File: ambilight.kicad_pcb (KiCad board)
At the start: 2 copper layers, 12 parts, among them J1 RGB Connector, J2 USB_C, J3 USB4085-GF-A, U1 ESP-01v090, U2 AZ1117CR-3.3TRG1, U2 LD1117V33, U3 FT230XS, U4 AZ1117CR-3.3TRG1

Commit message: Bunch of updates and beginning of PCB layout
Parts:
- removed the U2 at (94.0, 45.0)
- removed the U2 at (116.5, 45.1)
- removed U4: AZ1117CR-3.3TRG1, Package_TO_SOT_SMD:SOT-89-3_Handsoldering
- added C3: 0.1uF, Capacitor_SMD:C_0805_2012Metric, F.Cu at (62.5, 38.5)
- added C4: 0.1uF, Capacitor_SMD:C_0805_2012Metric, F.Cu at (62.5, 30.5)
- added C5: 10uF, Capacitor_SMD:C_0805_2012Metric, F.Cu at (62.5, 32.5)
- added C6: TBD, Capacitor_SMD:C_0805_2012Metric, F.Cu at (82.0, 34.7)
- added C7: TBD, Capacitor_SMD:C_0805_2012Metric, F.Cu at (82.0, 40.7)
- added C8: 0.1uF, Capacitor_SMD:C_0805_2012Metric, F.Cu at (108.0, 77.5)
- added C9: 1uF, Capacitor_SMD:C_0805_2012Metric, F.Cu at (108.5, 72.0)
- added D1: LED, LED_SMD:LED_0805_2012Metric, F.Cu at (86.0, 49.4)
- added R3: 120R, Resistor_SMD:R_0805_2012Metric, F.Cu at (84.0, 49.4)
- added R4: 10kR, Resistor_SMD:R_0805_2012Metric, F.Cu at (62.5, 36.5)
- added R5: 10kR, Resistor_SMD:R_0805_2012Metric, F.Cu at (62.5, 34.5)
- added R6: 10kR, Resistor_SMD:R_0805_2012Metric, F.Cu at (68.6, 42.0)
- added R7: 0R, Resistor_SMD:R_0805_2012Metric, F.Cu at (80.0, 36.7)
- added R8: 0R, Resistor_SMD:R_0805_2012Metric, F.Cu at (80.0, 38.7)
- added SW1: RESET, Button_Switch_SMD:SW_Push_1P1T_NO_CK_KMR2, F.Cu at (62.5, 44.8)
- added SW2: BOOT, Button_Switch_SMD:SW_Push_1P1T_NO_CK_KMR2, F.Cu at (68.5, 44.8)
- added TP1: ~, Custom_PCBWay:TestPoint_Pad_D2.5mm_SilkscreenFix, F.Cu at (89.0, 45.5)
- added TP2: ~, Custom_PCBWay:TestPoint_Pad_D2.5mm_SilkscreenFix, F.Cu at (80.0, 31.5)
- added TP3: ~, Custom_PCBWay:TestPoint_Pad_D2.5mm_SilkscreenFix, F.Cu at (86.0, 31.5)
- added TP4: ~, Custom_PCBWay:TestPoint_Pad_D2.5mm_SilkscreenFix, F.Cu at (107.0, 57.5)
- added TP5: ~, Custom_PCBWay:TestPoint_Pad_D2.5mm_SilkscreenFix, F.Cu at (119.0, 60.5)
- added U2: ESP32-C3-MINI-1-H4, PCM_Espressif:ESP32-C3-MINI-1, F.Cu at (71.2, 32.2)
- C1: value 100u -> 10uF; footprint Capacitor_THT:C_Rect_L9.0mm_W2.7mm_P7.50mm_MKT -> Capacitor_SMD:C_0805_2012Metric
- C2: value 47u -> 22uF; footprint Capacitor_THT:CP_Radial_D12.5mm_P5.00mm -> Capacitor_SMD:C_0805_2012Metric
- J1: value RGB Connector -> TYPE-C-31-M-12; footprint Connector_PinHeader_2.54mm:PinHeader_1x03_P2.54mm_Vertical -> Connector_USB:USB_C_Receptacle_HRO_TYPE-C-31-M-12
- J2: value USB_C -> RGB Connector; footprint Connector_USB:USB_C_Receptacle_GCT_USB4085 -> Connector_PinHeader_2.54mm:PinHeader_1x03_P2.54mm_Vertical
- J3: value USB4085-GF-A -> Power Connector; footprint Connector_USB:USB_C_Receptacle_GCT_USB4085 -> Connector_PinHeader_2.54mm:PinHeader_1x03_P2.54mm_Vertical
- R1: value 3.8R ? -> 5.1kR; footprint Resistor_THT:R_Axial_DIN0309_L9.0mm_D3.2mm_P2.54mm_Vertical -> Resistor_SMD:R_0805_2012Metric
- R2: value 5R ? -> 5.1kR; footprint Resistor_THT:R_Axial_DIN0309_L9.0mm_D3.2mm_P2.54mm_Vertical -> Resistor_SMD:R_0805_2012Metric
- U1: value ESP-01v090 -> AZ1117CR-3.3TRG1; footprint ESP8266:ESP-01 -> Package_TO_SOT_SMD:SOT-89-3_Handsoldering
- U3: value FT230XS -> MCP1416; footprint Package_SO:SSOP-16_3.9x4.9mm_P0.635mm -> Package_TO_SOT_SMD:SOT-23-5
- moved R2 100.6 mm to (85.4, 36.4), turned to 180 degrees
- moved R1 98.8 mm to (85.4, 39.0), turned to 180 degrees
- moved J1 71.7 mm to (92.5, 38.2), turned to 90 degrees
- moved C1 63.1 mm to (82.0, 49.5)
- moved U1 57.3 mm to (77.0, 49.0), turned to 180 degrees
- moved C2 56.5 mm to (72.5, 50.0), turned to -90 degrees
- moved J3 43.7 mm to (85.5, 58.0), turned to 90 degrees
- moved J2 31.6 mm to (95.0, 52.5), turned to 0 degrees
- moved U3 10.8 mm to (76.9, 42.5), turned to 180 degrees
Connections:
- C1 pad 1: Net-(J1-Pin_3) -> VCC
- C1 pad 2: Net-(J1-Pin_1) -> GND
- C2 pad 1: Net-(U1-VCC) -> +3V3
- C2 pad 2: Net-(J1-Pin_3) -> GND
- R1 pad 1: Net-(U1-VCC) -> Net-(J1-CC1)
- R1 pad 2: Net-(J1-Pin_2) -> GND
- R2 pad 1: Net-(U1-CH_PD) -> Net-(J1-CC2)
- R2 pad 2: Net-(U1-VCC) -> GND
- U1 pad 1: unconnected-(U1-UTXD-Pad1) -> GND
- U1 pad 2: Net-(J1-Pin_3) -> +3V3
- U1 pad 3: Net-(U1-CH_PD) -> VCC
- U3 pad 2: unconnected-(U3-~{RTS}-Pad2) -> VCC
- U3 pad 3: Net-(U3-3V3OUT) -> Net-(U2-GPIO4/ADC1_CH4)
- U3 pad 4: unconnected-(U3-RXD-Pad4) -> GND
- U3 pad 5: GND -> Net-(J2-Pin_2)
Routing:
- net +3V3: track 0.00 -> 55.6 mm
- net VCC: track 0.00 -> 29.1 mm
- net GND: track 0.00 -> 22.2 mm, vias 0 -> 9
- net Net-(U2-EN/CHIP_PU): track 0.00 -> 14.3 mm
- net /USBD+: track 0.00 -> 13.3 mm
- net /USBD-: track 0.00 -> 13.1 mm
- net Net-(U2-GPIO9): track 0.00 -> 10.6 mm
- net Net-(U2-GPIO20/U0RXD): track 0.00 -> 10.3 mm
- net Net-(U2-GPIO4/ADC1_CH4): track 0.00 -> 8.72 mm, vias 0 -> 2
- net Net-(U2-GPIO8): track 0.00 -> 6.17 mm
- net Net-(U2-GPIO21/U0TXD): track 0.00 -> 5.03 mm
- net Net-(J1-CC1): track 0.00 -> 2.31 mm
- net /D+: track 0.00 -> 2.23 mm
- net /D-: track 0.00 -> 2.21 mm
- net Net-(J1-CC2): track 0.00 -> 2.07 mm
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- added copper zone on B.Cu, net GND
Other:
- board outline added: 116 x 61.5 mm

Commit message: First draft of layout
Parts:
- TP4, TP5: footprint Custom_PCBWay:TestPoint_Pad_D2.5mm_SilkscreenFix -> TestPoint:TestPoint_Pad_D1.0mm
- moved TP5 50.5 mm to (70.0, 48.5)
- moved C8 41.6 mm to (83.8, 43.7), turned to -90 degrees
- moved C9 38.9 mm to (81.9, 43.7), turned to -90 degrees
- moved TP4 37.0 mm to (72.5, 44.0)
- moved J3 22.5 mm to (64.0, 51.3)
- moved J2 22.0 mm to (73.0, 51.3), turned to 90 degrees
- moved C1 2.26 mm to (81.9, 47.2)
- moved C2 2.26 mm to (72.5, 47.7)
- moved D1 2.26 mm to (85.9, 47.2)
- moved R3 2.26 mm to (83.9, 47.2)
- moved U1 2.26 mm to (77.0, 46.7)
- moved C5 2.00 mm to (62.5, 30.5)
- moved C4 2.00 mm to (62.5, 32.5)
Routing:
- net VCC: track 29.1 -> 56.1 mm
- net Net-(J2-Pin_2): track 0.00 -> 13.6 mm, vias 0 -> 2
- net GND: track 22.2 -> 34.7 mm, vias 9 -> 24
- net +3V3: track 55.6 -> 51.9 mm
- net Net-(U2-GPIO4/ADC1_CH4): track 8.72 -> 10.5 mm
- net Net-(U2-GPIO9): track 10.6 -> 11.3 mm
- added copper zone on F.Cu, net GND
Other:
- board text added: "Add ESD protection to data lines"
- board text added: "Flip places"

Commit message: Some reordering
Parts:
- moved MAIN 11.2 mm to (62.5, 47.5)
- moved R6 6.27 mm to (62.5, 40.5)
- moved TP5 1.85 mm to (70.4, 46.7)
- moved RST 1.57 mm to (63.0, 43.3)
- moved PWR 1.52 mm to (62.5, 51.1)
- moved BOOT 1.50 mm to (68.6, 43.3)
- renumbered SW2 to BOOT, J2 to MAIN, J3 to PWR, SW1 to RST
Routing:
- net Net-(U2-GPIO8): track 6.17 -> 12.4 mm
- net +3V3: track 51.9 -> 46.6 mm
- net VCC: track 56.1 -> 60.0 mm
- net Net-(J2-Pin_2): track 13.6 -> 17.1 mm
- net Net-(U2-GPIO9): track 11.3 -> 10.0 mm
- net Net-(U2-EN/CHIP_PU): track 14.3 -> 13.1 mm
- net GND: track 34.7 -> 35.2 mm

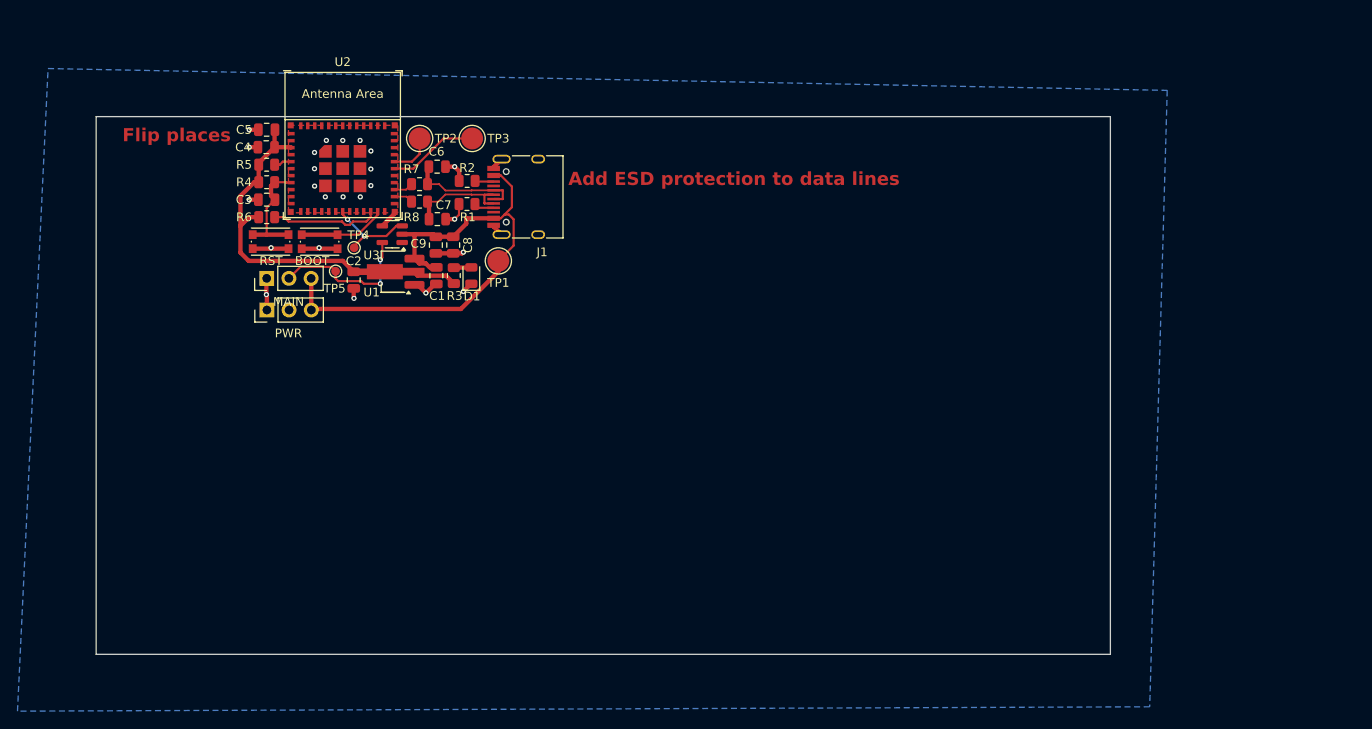
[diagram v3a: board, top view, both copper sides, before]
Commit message: Add ESD protection, reroute layout more efficiently
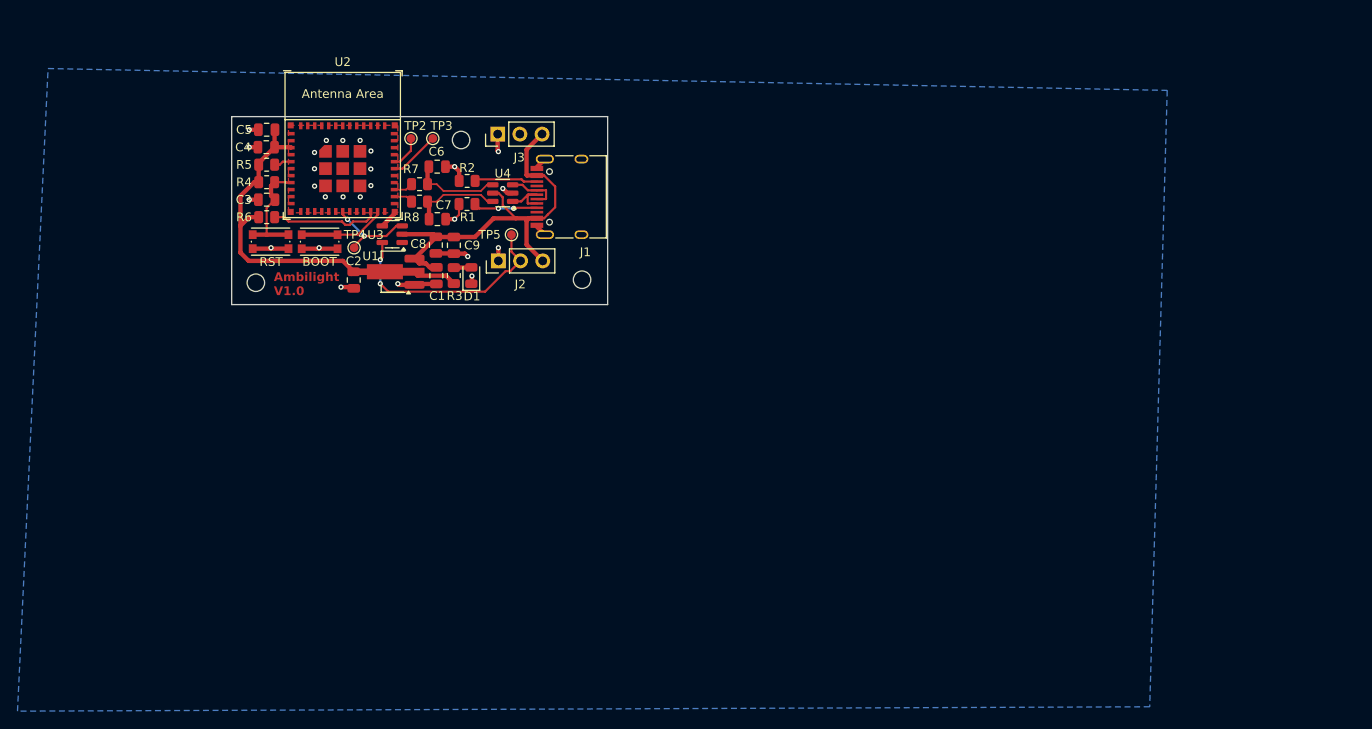
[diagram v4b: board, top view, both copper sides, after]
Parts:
- removed TP1: ~, Custom_PCBWay:TestPoint_Pad_D2.5mm_SilkscreenFix
- added REF**: MountingHole_2mm, MountingHole:MountingHole_2mm, F.Cu at (98.6, 47.7)
- added REF**: MountingHole_2mm, MountingHole:MountingHole_2mm, F.Cu at (61.3, 48.0)
- added REF**: MountingHole_2mm, MountingHole:MountingHole_2mm, F.Cu at (84.7, 31.7)
- added U4: USBLC6-2SC6, Package_TO_SOT_SMD:SOT-23-6, F.Cu at (89.5, 37.7)
- TP2, TP3: footprint Custom_PCBWay:TestPoint_Pad_D2.5mm_SilkscreenFix -> TestPoint:TestPoint_Pad_D1.0mm
- moved J3 33.2 mm to (88.9, 31.0)
- moved J2 26.6 mm to (89.0, 45.5)
- moved TP5 20.5 mm to (90.5, 42.5)
- moved J1 4.95 mm to (97.5, 38.2)
- moved TP3 4.50 mm to (81.5, 31.5)
- moved C9 2.06 mm to (83.9, 43.7)
- moved C8 1.98 mm to (81.9, 43.7)
- moved TP2 1.00 mm to (79.0, 31.5)
- renumbered MAIN to J2, PWR to J3
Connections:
- J1 pad A6: /USBD+ -> Net-(J1-D+-PadA6)
- J1 pad A7: /USBD- -> Net-(J1-D--PadA7)
- J1 pad B6: /USBD+ -> Net-(J1-D+-PadA6)
- J1 pad B7: /USBD- -> Net-(J1-D--PadA7)
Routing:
- net VCC: track 60.0 -> 47.2 mm
- net Net-(J2-Pin_2): track 17.1 -> 26.1 mm
- net Net-(J1-D--PadA7): track 0.00 -> 6.13 mm
- net Net-(J1-D+-PadA6): track 0.00 -> 6.10 mm
- net Net-(J1-CC2): track 2.07 -> 7.34 mm
- net Net-(J1-CC1): track 2.31 -> 7.32 mm, vias 0 -> 2
- net Net-(U2-GPIO20/U0RXD): track 10.3 -> 5.83 mm
- net GND: track 35.2 -> 38.3 mm, vias 24 -> 26
- net /USBD-: track 13.1 -> 10.2 mm
- net /USBD+: track 13.3 -> 10.5 mm
- net Net-(U2-GPIO21/U0TXD): track 5.03 -> 3.82 mm
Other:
- board size 116 x 61.5 mm -> 43 x 21.5 mm
- board text added: "Ambilight V1.0"
- board text removed: "Add ESD protection to data lines"
- board text removed: "Flip places"

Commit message: Minor layout adjustments
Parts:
- TP2, TP3, TP4, TP5: footprint TestPoint:TestPoint_Pad_D1.0mm -> Custom_PCBWay:TestPoint_Pad_D1.0mm_SilkscreenFix
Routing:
- net GND: track 38.3 -> 47.9 mm
- net Net-(U2-GPIO4/ADC1_CH4): track 10.5 -> 11.4 mm
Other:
- outline, holes or cut-outs redrawn
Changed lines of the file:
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@@
 		)
 	)
-	(footprint "TestPoint:TestPoint_Pad_D1.0mm"
+	(footprint "Custom_PCBWay:TestPoint_Pad_D1.0mm_SilkscreenFix"
 		(layer "F.Cu")
 		(at 79 31.5)
@@
 		(tags "test point SMD pad")
 		(property "Reference" "TP2"
-			(at 0.5 -1.448 0)
+			(at 0.423759 -1.414643 0)
 			(layer "F.SilkS")
 			(effects
@@
 		(fp_circle
 			(center 0 0)
-			(end 0 0.7)
+			(end 0.75 0)
 			(stroke
 				(width 0.12)
@@
 		)
 	)
-	(footprint "TestPoint:TestPoint_Pad_D1.0mm"
+	(footprint "Custom_PCBWay:TestPoint_Pad_D1.0mm_SilkscreenFix"
 		(layer "F.Cu")
 		(at 72.5 44)
@@
 		(tags "test point SMD pad")
 		(property "Reference" "TP4"
-			(at 0.086568 -1.495139 0)
+			(at 0.305352 -1.405768 0)
 			(layer "F.SilkS")
 			(effects
@@
 		(fp_circle
 			(center 0 0)
-			(end 0 0.7)
+			(end 0.75 0)
 			(stroke
 				(width 0.12)
@@
 		(tags "SOT TO_SOT_SMD")
 		(property "Reference" "U3"
-			(at 1.91031 -0.078168 0)
+			(at 3.045306 1.082736 0)
 			(layer "F.SilkS")
 			(effects
@@
 		(embedded_fonts no)
 	)
-	(footprint "TestPoint:TestPoint_Pad_D1.0mm"
+	(footprint "Custom_PCBWay:TestPoint_Pad_D1.0mm_SilkscreenFix"
 		(layer "F.Cu")
 		(at 81.5 31.5)
@@
 		(tags "test point SMD pad")
 		(property "Reference" "TP3"
-			(at 1 -1.448 0)
+			(at 0.902818 -1.392977 0)
 			(layer "F.SilkS")
 			(effects
@@
 		(fp_circle
 			(center 0 0)
-			(end 0 0.7)
+			(end 0.75 0)
 			(stroke
 				(width 0.12)
@@
 		(tags "SOT-89-3 Handsoldering")
 		(property "Reference" "U1"
-			(at 2.572396 1.783654 0)
+			(at 2.684477 1.699522 0)
 			(layer "F.SilkS")
 			(effects
@@
 		(embedded_fonts no)
 	)
-	(footprint "TestPoint:TestPoint_Pad_D1.0mm"
+	(footprint "Custom_PCBWay:TestPoint_Pad_D1.0mm_SilkscreenFix"
 		(layer "F.Cu")
 		(at 90.5 42.5)
@@
 		(tags "test point SMD pad")
 		(property "Reference" "TP5"
-			(at -2.5 0 0)
+			(at 0 -1.448 0)
 			(layer "F.SilkS")
 			(effects
@@
 		(fp_circle
 			(center 0 0)
-			(end 0 0.7)
+			(end 0.75 0)
 			(stroke
 				(width 0.12)
@@
 		(embedded_fonts no)
 	)
-	(gr_rect
-		(start 58.5 29)
-		(end 101.5 50.5)
+	(gr_line
+		(start 101.5 30)
+		(end 101.5 49.5)
+		(stroke
+			(width 0.05)
+			(type default)
+		)
+		(layer "Edge.Cuts")
+	)
+	(gr_line
+		(start 58.5 49.5)
+		(end 58.5 30)
+		(stroke
+			(width 0.05)
+			(type default)
+		)
+		(layer "Edge.Cuts")
+	)
+	(gr_arc
+		(start 59.5 50.5)
+		(mid 58.792893 50.207107)
+		(end 58.5 49.5)
+		(stroke
+			(width 0.05)
+			(type default)
+		)
+		(layer "Edge.Cuts")
+	)
+	(gr_line
+		(start 100.5 50.5)
+		(end 59.5 50.5)
+		(stroke
+			(width 0.05)
+			(type default)
+		)
+		(layer "Edge.Cuts")
+	)
+	(gr_arc
+		(start 101.5 49.5)
+		(mid 101.207107 50.207107)
+		(end 100.5 50.5)
+		(stroke
+			(width 0.05)
+			(type default)
+		)
+		(layer "Edge.Cuts")
+	)
+	(gr_arc
+		(start 58.5 30)
+		(mid 58.792893 29.292893)
+		(end 59.5 29)
+		(stroke
+			(width 0.05)
+			(type default)
+		)
+		(layer "Edge.Cuts")
+	)
+	(gr_arc
+		(start 100.5 29)
+		(mid 101.207107 29.292893)
+		(end 101.5 30)
+		(stroke
+			(width 0.05)
+			(type default)
+		)
+		(layer "Edge.Cuts")
+	)
+	(gr_line
+		(start 59.5 29)
+		(end 100.5 29)
 		(stroke
 			(width 0.05)
 			(type default)
 		)
-		(fill no)
 		(layer "Edge.Cuts")
 	)
@@
 	)
 	(segment
-		(start 90.820886 39.43)
-		(end 90.752385 39.498501)
-		(width 0.25)
-		(layer "F.Cu")
-		(net 6)
-	)
-	(segment
-		(start 88.997598 39.501777)
-		(end 86.826777 39.501777)
+		(start 91.5 39.43)
+		(end 93.405 39.43)
 		(width 0.25)
 		(layer "F.Cu")
@@
 	)
 	(segment
-		(start 93.405 39.43)
-		(end 90.820886 39.43)
+		(start 88 39.501777)
+		(end 86.826777 39.501777)
 		(width 0.25)
 		(layer "F.Cu")
@@
 	)
 	(via
-		(at 90.752385 39.498501)
+		(at 91.5 39.43)
 		(size 0.6)
 		(drill 0.3)
@@
 	)
 	(via
-		(at 88.997598 39.501777)
+		(at 88 39.501777)
 		(size 0.6)
 		(drill 0.3)
@@
 	)
 	(segment
+		(start 91.431499 39.498501)
+		(end 91.5 39.43)
+		(width 0.25)
+		(layer "B.Cu")
+		(net 6)
+	)
+	(segment
 		(start 89.000874 39.498501)
+		(end 91.431499 39.498501)
+		(width 0.25)
+		(layer "B.Cu")
+		(net 6)
+	)
+	(segment
+		(start 88 39.501777)
 		(end 88.997598 39.501777)
 		(width 0.25)
@@
 	)
 	(segment
-		(start 90.752385 39.498501)
+		(start 88.997598 39.501777)
 		(end 89.000874 39.498501)
 		(width 0.25)
@@
 	)
 	(segment
-		(start 76.178272 42.659229)
-		(end 77.337501 41.5)
+		(start 73.5 44)
+		(end 72.5 44)
 		(width 0.25)
 		(layer "F.Cu")
@@
 	)
 	(segment
-		(start 77.337501 41.5)
-		(end 78 41.5)
+		(start 71.75 40.75)
+		(end 71.2 40.2)
 		(width 0.25)
 		(layer "F.Cu")
@@
 	)
 	(segment
-		(start 72.5 43.818457)
-		(end 73.659228 42.659229)
+		(start 74.5 42.659229)
+		(end 76.178272 42.659229)
 		(width 0.25)
 		(layer "F.Cu")
@@
 	)
 	(segment
-		(start 71.75 40.75)
-		(end 71.2 40.2)
+		(start 76.178272 42.659229)
+		(end 77.337501 41.5)
 		(width 0.25)
 		(layer "F.Cu")
@@
 	)
 	(segment
-		(start 73.659228 42.659229)
-		(end 76.178272 42.659229)
+		(start 71.2 40.2)
+		(end 71.2 39.85)
 		(width 0.25)
 		(layer "F.Cu")
@@
 	)
 	(segment
-		(start 71.2 40.2)
-		(end 71.2 39.85)
+		(start 77.337501 41.5)
+		(end 78 41.5)
+		(width 0.25)
+		(layer "F.Cu")
+		(net 17)
+	)
+	(segment
+		(start 74.5 43)
+		(end 73.5 44)
 		(width 0.25)
 		(layer "F.Cu")
@@
 	)
 	(segment
-		(start 72.5 44)
-		(end 72.5 43.818457)
+		(start 74.5 42.659229)
+		(end 74.5 43)
 		(width 0.25)
 		(layer "F.Cu")
@@
 	)
 	(via
-		(at 73.659228 42.659229)
+		(at 74.5 42.659229)
 		(size 0.6)
 		(drill 0.3)
@@
 	)
 	(segment
+		(start 73.659229 42.659229)
+		(end 74.5 42.659229)
+		(width 0.25)
+		(layer "B.Cu")
+		(net 17)
+	)
+	(segment
 		(start 71.75 40.75)
-		(end 73.659228 42.659229)
+		(end 73.659229 42.659229)
 		(width 0.25)
 		(layer "B.Cu")
@@
 	)
 	(segment
+		(start 61.5 32.5)
+		(end 60.5 33.5)
+		(width 0.5)
+		(layer "F.Cu")
+		(net 18)
+	)
+	(segment
 		(start 88.92 31)
 		(end 88.92 32.92)
@@
 	)
 	(segment
+		(start 94.32 33.86)
+		(end 98.5 33.86)
+		(width 0.5)
+		(layer "F.Cu")
+		(net 18)
+	)
+	(segment
 		(start 71 48.5)
 		(end 72.314856 48.5)
@@
 	)
 	(segment
+		(start 61.5 38.5)
+		(end 60.5 39.5)
+		(width 0.5)
+		(layer "F.Cu")
+		(net 18)
+	)
+	(segment
 		(start 77.6285 48.242853)
 		(end 77.5 48.114353)
@@
 	)
 	(segment
-		(start 61.55 38.5)
-		(end 60.5 38.5)
-		(width 0.5)
-		(layer "F.Cu")
-		(net 18)
-	)
-	(segment
-		(start 61.5 30.5)
-		(end 60.5 30.5)
+		(start 63.1 44.1)
+		(end 63 44)
 		(width 0.5)
 		(layer "F.Cu")
@@
 	)
 	(segment
-		(start 63.1 44.1)
-		(end 63 44)
+		(start 93.405 41.585)
+		(end 94.32 42.5)
 		(width 0.5)
 		(layer "F.Cu")
@@
 	)
 	(segment
-		(start 93.405 41.585)
-		(end 94.32 42.5)
+		(start 94.32 42.5)
+		(end 98.5 42.5)
 		(width 0.5)
 		(layer "F.Cu")
@@
 	)
 	(segment
+		(start 61.55 38.5)
+		(end 61.5 38.5)
+		(width 0.5)
+		(layer "F.Cu")
+		(net 18)
+	)
+	(segment
 		(start 79.407709 48.242853)
 		(end 79.785212 48.242853)
@@
 	)
 	(segment
-		(start 61.5 32.5)
-		(end 60.5 32.5)
+		(start 61.5 30.5)
+		(end 60.5 31.5)
 		(width 0.5)
 		(layer "F.Cu")
@@
 	)
 	(via
-		(at 60.5 32.5)
+		(at 60.5 33.5)
 		(size 0.6)
 		(drill 0.3)
@@
 	)
 	(via
-		(at 60.5 30.5)
+		(at 60.5 31.5)
 		(size 0.6)
 		(drill 0.3)
@@
 	)
 	(via
-		(at 60.5 38.5)
+		(at 60.5 39.5)
 		(size 0.6)
 		(drill 0.3)
